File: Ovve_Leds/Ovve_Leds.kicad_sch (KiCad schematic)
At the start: 6 parts, among them J2 Conn_01x04, J3 Conn_01x04, J4 Conn_01x04, J5 Conn_01x04, J6 Conn_01x04, J7 Conn_01x04

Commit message: Finished preliminary schematics
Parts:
- added J8: Conn_01x02, symbol Connector_Generic:Conn_01x02
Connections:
- new net Arduino_Power_A_letter/6V_in: J8.2 (Pin_2)
- new net Arduino_Power_A_letter/GND_in: J8.1 (Pin_1)
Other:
- sheet Arduino_Power_A_letter ports: added 6V_in, GND_in; removed none
- note added: "Connect 6V (i.e. 4 1,5V AA batteries) here"
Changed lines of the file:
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@@
+	(wire
+		(pts
+			(xy 59.69 45.72) (xy 59.69 48.26)
+		)
+		(stroke
+			(width 0)
+			(type default)
+		)
+	)
 	(wire
 		(pts
@@
 	(wire
 		(pts
+			(xy 62.23 45.72) (xy 62.23 48.26)
+		)
+		(stroke
+			(width 0)
+			(type default)
+		)
+	)
+	(wire
+		(pts
 			(xy 168.91 73.66) (xy 170.18 73.66)
 		)
@@
 			(width 0)
 			(type default)
+		)
+	)
+	(text "Connect 6V (i.e. 4 1,5V AA batteries) here \n"
+		(exclude_from_sim no)
+		(at 61.468 35.052 0)
+		(effects
+			(font
+				(size 1.27 1.27)
+			)
 		)
 	)
@@
 	)
 	(symbol
+		(lib_id "Connector_Generic:Conn_01x02")
+		(at 59.69 40.64 90)
+		(unit 1)
+		(exclude_from_sim no)
+		(in_bom yes)
+		(on_board yes)
+		(dnp no)
+		(fields_autoplaced yes)
+		(property "Reference" "J8"
+			(at 64.77 39.3699 90)
+			(effects
+				(font
+					(size 1.27 1.27)
+				)
+				(justify right)
+			)
+		)
+		(property "Value" "Conn_01x02"
+			(at 64.77 41.9099 90)
+			(effects
+				(font
+					(size 1.27 1.27)
+				)
+				(justify right)
+			)
+		)
+		(property "Footprint" ""
+			(at 59.69 40.64 0)
+			(effects
+				(font
+					(size 1.27 1.27)
+				)
+				(hide yes)
+			)
+		)
+		(property "Datasheet" "~"
+			(at 59.69 40.64 0)
+			(effects
+				(font
+					(size 1.27 1.27)
+				)
+				(hide yes)
+			)
+		)
+		(property "Description" "Generic connector, single row, 01x02, script generated (kicad-library-utils/schlib/autogen/connector/)"
+			(at 59.69 40.64 0)
+			(effects
+				(font
+					(size 1.27 1.27)
+				)
+				(hide yes)
+			)
+		)
+		(pin "1"
+		)
+		(pin "2"
+		)
+		(instances
+			(project "Ovve_Leds"
+				(path "/a3f154e4-ded7-4c3a-b779-1e1dc74aad12"
+					(reference "J8")
+					(unit 1)
+				)
+			)
+		)
+	)
+	(symbol
 		(lib_id "Connector_Generic:Conn_01x04")
 		(at 93.98 73.66 180)
@@
 			(effects
 				(font
+					(size 1.27 1.27)
+				)
+				(justify right)
+			)
+		)
+		(pin "GND_in" input
+			(at 59.69 48.26 90)
+			(effects
+				(font
+					(size 1.27 1.27)
+				)
+				(justify right)
+			)
+		)
+		(pin "6V_in" input
+			(at 62.23 48.26 90)
+			(effects
+				(font

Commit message: Added decoupling capacitors and assigned footprints
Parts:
- J2, J3, J4, J5, J6, J7, J8: footprint (none) -> Connector_PinHeader_2.54mm:PinHeader_1x04_P2.54mm_Horizontal
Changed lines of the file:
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@@
 			)
 		)
-		(property "Footprint" ""
+		(property "Footprint" "Connector_PinHeader_2.54mm:PinHeader_1x04_P2.54mm_Horizontal"
 			(at 163.83 73.66 0)
 			(effects
@@
 			)
 		)
-		(property "Footprint" ""
+		(property "Footprint" "Connector_PinHeader_2.54mm:PinHeader_1x04_P2.54mm_Horizontal"
 			(at 222.25 69.85 0)
 			(effects
@@
 			)
 		)
-		(property "Footprint" ""
+		(property "Footprint" "Connector_PinHeader_2.54mm:PinHeader_1x04_P2.54mm_Horizontal"
 			(at 232.41 72.39 0)
 			(effects
@@
 			)
 		)
-		(property "Footprint" ""
+		(property "Footprint" "Connector_PinHeader_2.54mm:PinHeader_1x04_P2.54mm_Horizontal"
 			(at 59.69 40.64 0)
 			(effects
@@
 			)
 		)
-		(property "Footprint" ""
+		(property "Footprint" "Connector_PinHeader_2.54mm:PinHeader_1x04_P2.54mm_Horizontal"
 			(at 93.98 73.66 0)
 			(effects
@@
 			)
 		)
-		(property "Footprint" ""
+		(property "Footprint" "Connector_PinHeader_2.54mm:PinHeader_1x04_P2.54mm_Horizontal"
 			(at 83.82 71.12 0)
 			(effects
@@
 			)
 		)
-		(property "Footprint" ""
+		(property "Footprint" "Connector_PinHeader_2.54mm:PinHeader_1x04_P2.54mm_Horizontal"
 			(at 153.67 71.12 0)
 			(effects

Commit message: updated footprint of connector
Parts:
- J8: footprint Connector_PinHeader_2.54mm:PinHeader_1x04_P2.54mm_Horizontal -> Connector_PinHeader_2.54mm:PinHeader_1x02_P2.54mm_Horizontal
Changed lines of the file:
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@@
 			)
 		)
-		(property "Footprint" "Connector_PinHeader_2.54mm:PinHeader_1x04_P2.54mm_Horizontal"
+		(property "Footprint" "Connector_PinHeader_2.54mm:PinHeader_1x02_P2.54mm_Horizontal"
 			(at 59.69 40.64 0)
 			(effects

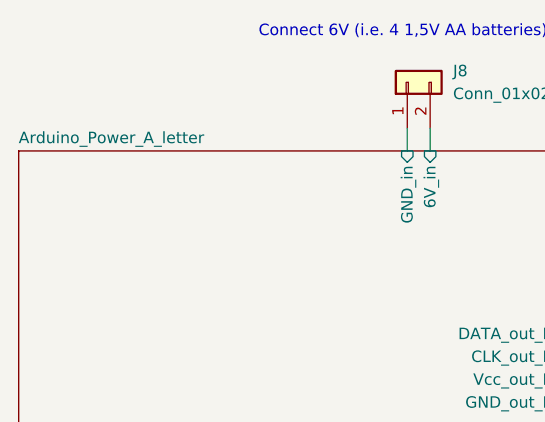
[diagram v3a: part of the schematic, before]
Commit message: Updated flip-flops
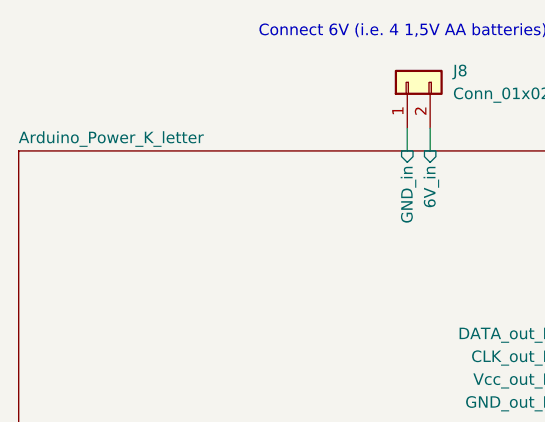
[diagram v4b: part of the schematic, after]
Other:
- sheet Arduino_Power_A_letter renamed Arduino_Power_K_letter
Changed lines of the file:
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@@
 			(color 0 0 0 0.0000)
 		)
-		(property "Sheetname" "Arduino_Power_A_letter"
+		(property "Sheetname" "Arduino_Power_K_letter"
 			(at 16.51 47.5484 0)
 			(effects

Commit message: Started work on new design with only one letter
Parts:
- removed J5, J6, J7: Conn_01x04, Connector_PinHeader_2.54mm:PinHeader_1x04_P2.54mm_Horizontal, symbol Connector_Generic:Conn_01x04
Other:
- removed sheet L_letter
- removed sheet R_letter

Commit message: Preliminarily finished with routing letter
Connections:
- net A_letter/CLK_in_A renamed A_letter/CLK_in
- net A_letter/CLK_out_A renamed A_letter/CLK_out
- net A_letter/DATA_in_A renamed A_letter/DATA_in
- net A_letter/DATA_out_A renamed A_letter/DATA_out
- net A_letter/GND_in_A renamed A_letter/GND_in
- net A_letter/GND_out_A renamed A_letter/GND_out
- net A_letter/Vcc_in_A renamed A_letter/Vcc_in
- net A_letter/Vcc_out_A renamed A_letter/Vcc_out
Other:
- sheet A_letter ports: added CLK_in, CLK_out, DATA_in, DATA_out, GND_in, GND_out, Vcc_in, Vcc_out; removed CLK_in_A, CLK_out_A, DATA_in_A, DATA_out_A, GND_in_A, GND_out_A, Vcc_in_A, Vcc_out_A
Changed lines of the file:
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@@
 			)
 		)
-		(pin "DATA_in_A" input
+		(pin "DATA_in" input
 			(at 100.33 68.58 180)
 			(effects
@@
 			)
 		)
-		(pin "CLK_in_A" input
+		(pin "CLK_in" input
 			(at 100.33 71.12 180)
 			(effects
@@
 			)
 		)
-		(pin "Vcc_in_A" input
+		(pin "Vcc_in" input
 			(at 100.33 73.66 180)
 			(effects
@@
 			)
 		)
-		(pin "GND_in_A" input
+		(pin "GND_in" input
 			(at 100.33 76.2 180)
 			(effects
@@
 			)
 		)
-		(pin "Vcc_out_A" output
+		(pin "Vcc_out" output
 			(at 147.32 73.66 0)
 			(effects
@@
 			)
 		)
-		(pin "DATA_out_A" output
+		(pin "DATA_out" output
 			(at 147.32 68.58 0)
 			(effects
@@
 			)
 		)
-		(pin "CLK_out_A" output
+		(pin "CLK_out" output
 			(at 147.32 71.12 0)
 			(effects
@@
 			)
 		)
-		(pin "GND_out_A" output
+		(pin "GND_out" output
 			(at 147.32 76.2 0)
 			(effects
